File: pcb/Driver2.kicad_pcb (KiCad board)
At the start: 2 copper layers, 78 x 124 mm, 41 parts, among them P1 CONN_2, P2 CONN_2, Q1 RPF60N06, Q2 RPF60N06, Q3 IRF540N, T1 ETD29, U1 ArdinoMinPro, U2 MCP14E4, U3 LM7808ACT

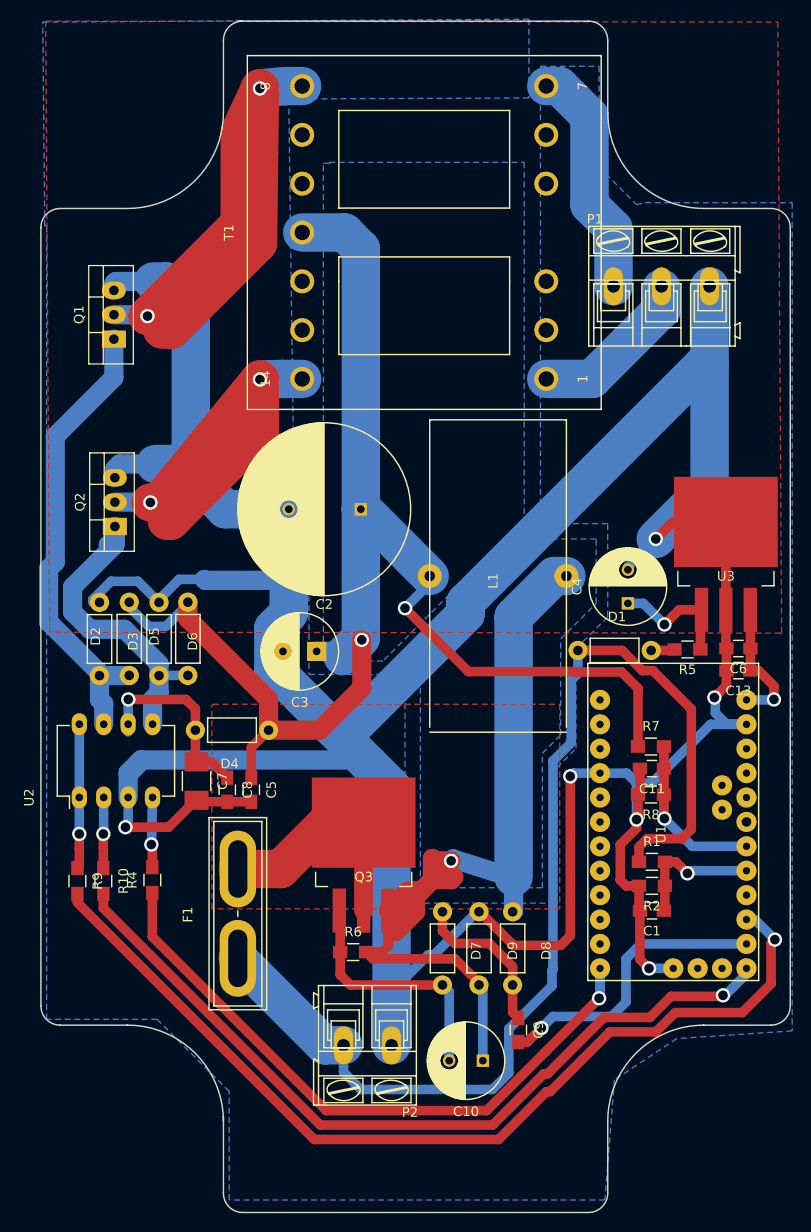
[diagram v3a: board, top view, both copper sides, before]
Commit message: v2 board complete with temperature sensor on power components
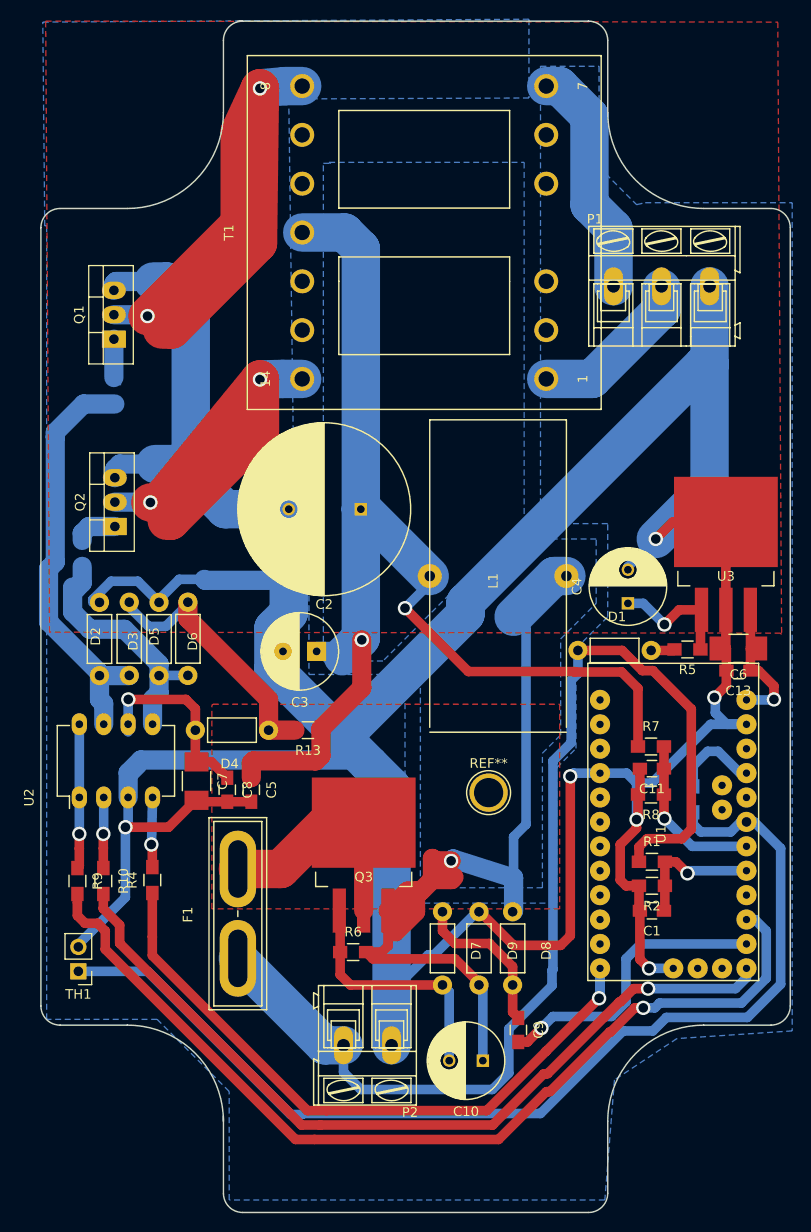
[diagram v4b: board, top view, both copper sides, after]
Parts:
- added R11: 0R, Resistors_SMD:R_0805_HandSoldering, B.Cu at (106.2, 94.0)
- added R12: 0R, Resistors_SMD:R_0805_HandSoldering, B.Cu at (102.8, 110.9)
- added R13: 0R, Resistors_SMD:R_0805_HandSoldering, F.Cu at (126.3, 129.3)
- added R3: 10K, Resistors_SMD:R_0805_HandSoldering, B.Cu at (166.4, 136.5)
- added REF**: 1pin, Connect:1pin, F.Cu at (145.1, 135.8)
- added TH1: MF52-103 Thermistor 10K, Pin_Headers:Pin_Header_Straight_1x02_Pitch2.54mm, F.Cu at (102.4, 154.4)
- C6: footprint Capacitors_SMD:C_0805_HandSoldering -> Capacitors_SMD:C_1210_HandSoldering
- Q3: value IRF540N -> IRL540
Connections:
- D2 pad 2: 12vPower -> Net-(D2-Pad2)
- D4 pad 1: 12vPower -> Net-(D2-Pad2)
- D5 pad 2: 12vPower -> Net-(D2-Pad2)
- Q1 pad 1: Net-(D2-Pad1) -> Net-(Q1-Pad1)
- Q2 pad 1: Net-(D5-Pad1) -> Net-(Q2-Pad1)
- U1 pad 19: (no net) -> ADC3
- U1 pad 21: (no net) -> 5v
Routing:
- net ADC3: track 0.00 -> 111.3 mm
- net Net-(D2-Pad2): track 0.00 -> 28.4 mm
- net 12vPower: track 150.4 -> 125.5 mm
- net GND: track 416.7 -> 431.2 mm
- net 5v: track 0.00 -> 9.25 mm
- net Net-(D5-Pad1): track 34.5 -> 26.4 mm
- net Net-(D2-Pad1): track 48.4 -> 43.7 mm
- net Net-(Q2-Pad1): track 0.00 -> 4.44 mm
- net Net-(Q1-Pad1): track 0.00 -> 4.00 mm
- net Net-(R10-Pad2): track 84.9 -> 86.8 mm
- net Net-(R9-Pad2): track 98.6 -> 100.0 mm
- net Net-(C10-Pad1): track 92.7 -> 93.9 mm
- net Net-(R4-Pad1): track 69.6 -> 70.8 mm
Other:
- net class 2m added: clearance 0.5, trace_width 2, via_dia 1.5, via_drill 1
- net class 4m added: clearance 0.5, trace_width 4, via_dia 1.5, via_drill 1
- net class Default: trace_width 2 -> 1

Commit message: v3, targetting 20-30KHz with 27KHz transducers
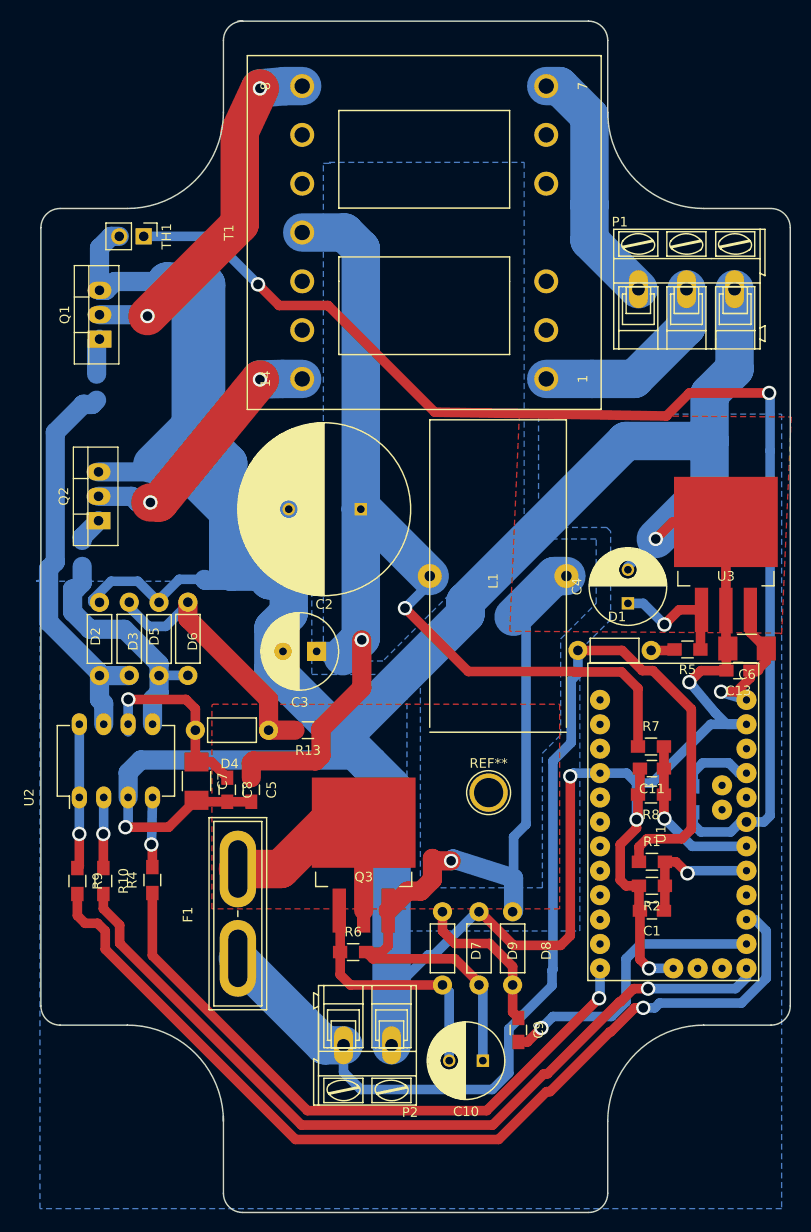
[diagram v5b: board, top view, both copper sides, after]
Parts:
- moved TH1 76.8 mm to (109.2, 77.9), turned to 270 degrees
- moved P1 2.62 mm to (160.7, 83.4)
- moved R11 1.94 mm to (104.3, 93.6)
- moved Q2 1.80 mm to (104.5, 107.5)
- moved Q1 1.50 mm to (104.6, 88.6)
- moved C6 0.90 mm to (172.0, 120.8)
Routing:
- net GND: track 431.2 -> 481.6 mm
- net Net-(Q1-Pad2): track 65.9 -> 37.8 mm
- net ADC3: track 111.3 -> 129.1 mm, vias 0 -> 2
- net Net-(Q2-Pad2): track 44.5 -> 27.6 mm
- net Net-(C10-Pad1): track 93.9 -> 83.7 mm
- net Net-(P1-Pad2): track 17.2 -> 20.8 mm
- net Net-(R4-Pad1): track 70.8 -> 67.7 mm
- net 8v: track 13.7 -> 16.2 mm
- net Net-(D2-Pad1): track 43.7 -> 41.9 mm
- net Net-(Q2-Pad1): track 4.44 -> 2.75 mm
- net Net-(P1-Pad1): track 24.5 -> 25.9 mm
- net Net-(R9-Pad2): track 100.0 -> 99.1 mm
- net 5v: track 9.25 -> 8.52 mm
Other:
- net class Default: trace_width 1 -> 4
